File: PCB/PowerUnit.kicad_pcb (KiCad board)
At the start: 2 copper layers, 0 parts

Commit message: added some components
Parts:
- added C1: 1u, erp:C_0805_2012Metric, F.Cu at (205.0, 120.0)
- added C10: 10n, erp:C_0805_2012Metric, F.Cu at (187.4, 118.3)
- added C11: 10n, erp:C_0805_2012Metric, F.Cu at (187.4, 115.4)
- added C12: 10n, erp:C_0805_2012Metric, F.Cu at (197.2, 107.1)
- added C13: 10n, erp:C_0805_2012Metric, F.Cu at (203.5, 102.3)
- added C14: 1u, erp:C_0805_2012Metric, F.Cu at (192.8, 113.3)
- added C15: 220n, erp:C_0805_2012Metric, F.Cu at (197.2, 110.0)
- added C2: 10n, erp:C_0805_2012Metric, F.Cu at (238.0, 104.0)
- added C3: 10n, erp:C_0805_2012Metric, F.Cu at (182.4, 126.7)
- added C4: 100n, erp:C_0805_2012Metric, F.Cu at (191.8, 116.3)
- added C5: 10n, erp:C_0805_2012Metric, F.Cu at (201.6, 105.2)
- added C6: 10n, erp:C_0805_2012Metric, F.Cu at (187.4, 121.3)
- added C7: 10n, erp:C_0805_2012Metric, F.Cu at (211.7, 96.0)
- added C8: 10n, erp:C_0805_2012Metric, F.Cu at (208.0, 99.0)
- added C9: 10u, erp:CP_EIA-6032-15_Kemet-U, F.Cu at (154.4, 125.9)
- added D1: 5.1V, erp:D_MiniMELF, F.Cu at (161.8, 128.4)
- added D19: LL4148, erp:D_MiniMELF, F.Cu at (187.4, 109.0)
- added D2: 5.1V, erp:D_MiniMELF, F.Cu at (201.8, 92.9)
- added D20: LL4148, erp:D_MiniMELF, F.Cu at (168.2, 128.4)
- added D21: LL4148, erp:D_MiniMELF, F.Cu at (198.1, 101.0)
- added D22: LL4148, erp:D_MiniMELF, F.Cu at (177.5, 120.5)
- added D23: GREEN, erp:LED_0805_2012Metric, F.Cu at (192.8, 110.3)
- added D24: RED, erp:LED_0805_2012Metric, F.Cu at (203.6, 99.3)
- added D25: RED, erp:LED_0805_2012Metric, F.Cu at (197.2, 104.1)
- added D26: RED, erp:LED_0805_2012Metric, F.Cu at (178.0, 123.7)
- added D27: RED, erp:LED_0805_2012Metric, F.Cu at (192.8, 107.3)
- added D30: LL4148, erp:D_MiniMELF, F.Cu at (187.4, 112.3)
- added D31: LL4148, erp:D_MiniMELF, F.Cu at (205.0, 81.0)
- added D32: LL4148, erp:D_MiniMELF, F.Cu at (201.8, 96.2)
- added D33: LL4148, erp:D_MiniMELF, F.Cu at (161.8, 125.1)
- added D34: RED, erp:LED_0805_2012Metric, F.Cu at (207.2, 96.1)
- added D35: RED, erp:LED_0805_2012Metric, F.Cu at (229.0, 90.0)
- added D36: RED, erp:LED_0805_2012Metric, F.Cu at (182.5, 123.7)
- added D37: RED, erp:LED_0805_2012Metric, F.Cu at (178.0, 126.7)
- added D8: LL4148, erp:D_MiniMELF, F.Cu at (168.2, 125.1)
- added D9: LL4148, erp:D_MiniMELF, F.Cu at (177.5, 117.3)
- added Q1: BC847C, erp:SOT-23, F.Cu at (182.9, 117.9)
- added Q10: STD45P4LLF6AG, erp:TO-252-3_TabPin2, F.Cu at (156.1, 111.4)
- added Q11: STD45P4LLF6AG, erp:TO-252-3_TabPin2, F.Cu at (165.6, 71.5)
- added Q12: STD15P6F6AG, erp:TO-252-3_TabPin2, F.Cu at (156.1, 103.4)
- added Q13: STD15P6F6AG, erp:TO-252-3_TabPin2, F.Cu at (149.6, 83.5)
- added Q2: STD15P6F6AG, erp:TO-252-3_TabPin2, F.Cu at (168.3, 119.5)
- added Q3: STD45P4LLF6AG, erp:TO-252-3_TabPin2, F.Cu at (192.6, 95.3)
- added Q4: STD45P4LLF6AG, erp:TO-252-3_TabPin2, F.Cu at (180.4, 103.4)
- added Q5: STD15P6F6AG, erp:TO-252-3_TabPin2, F.Cu at (168.3, 111.4)
- added Q6: STD15P6F6AG, erp:TO-252-3_TabPin2, F.Cu at (156.1, 119.5)
- added Q7: STD45P4LLF6AG, erp:TO-252-3_TabPin2, F.Cu at (186.6, 73.5)
- added Q8: BC847C, erp:SOT-23, F.Cu at (173.6, 125.8)
- added Q9: STD15P6F6AG, erp:TO-252-3_TabPin2, F.Cu at (168.3, 103.4)
- added R1: 2.2k, erp:R_0805_2012Metric, F.Cu at (231.0, 121.0)
- added R10: 820, erp:R_0805_2012Metric, F.Cu at (201.6, 111.2)
- added R11: 820, erp:R_0805_2012Metric, F.Cu at (196.2, 116.3)
- added R12: 820, erp:R_0805_2012Metric, F.Cu at (186.9, 127.2)
- added R13: 1k, erp:R_0805_2012Metric, F.Cu at (206.0, 108.2)
- added R14: 2.2k, erp:R_0805_2012Metric, F.Cu at (191.8, 122.2)
- added R15: 2.2k, erp:R_0805_2012Metric, F.Cu at (212.4, 101.9)
- added R16: 2.2k, erp:R_0805_2012Metric, F.Cu at (216.8, 98.8)
- added R17: 820, erp:R_0805_2012Metric, F.Cu at (196.2, 119.2)
- added R18: 820, erp:R_0805_2012Metric, F.Cu at (201.6, 114.1)
- added R19: 2.2k, erp:R_0805_2012Metric, F.Cu at (210.4, 105.0)
- added R2: 2.2k, erp:R_0805_2012Metric, F.Cu at (201.6, 108.2)
- added R20: 2.2k, erp:R_0805_2012Metric, F.Cu at (206.0, 111.2)
- added R21: 820, erp:R_0805_2012Metric, F.Cu at (191.3, 125.1)
- added R22: 820, erp:R_0805_2012Metric, F.Cu at (210.4, 107.9)
- added R23: 820, erp:R_0805_2012Metric, F.Cu at (196.2, 122.2)
- added R24: 2.2k, erp:R_0805_2012Metric, F.Cu at (216.8, 101.7)
- added R25: 2.2k, erp:R_0805_2012Metric, F.Cu at (200.6, 117.0)
- added R26: 2.2k, erp:R_0805_2012Metric, F.Cu at (191.3, 128.1)
- added R27: 2.2k, erp:R_0805_2012Metric, F.Cu at (214.8, 104.9)
- added R28: 560, erp:R_0805_2012Metric, F.Cu at (206.0, 114.1)
- added R29: 2.2k, erp:R_0805_2012Metric, F.Cu at (210.4, 110.8)
- added R3: 2.2k, erp:R_0805_2012Metric, F.Cu at (197.2, 113.0)
- added R30: 2.2k, erp:R_0805_2012Metric, F.Cu at (200.6, 120.0)
- added R31: 2.2k, erp:R_0805_2012Metric, F.Cu at (195.7, 125.1)
- added R32: 2.2k, erp:R_0805_2012Metric, F.Cu at (214.8, 107.8)
- added R33: 2.2k, erp:R_0805_2012Metric, F.Cu at (205.0, 117.0)
- added R34: 2.2k, erp:R_0805_2012Metric, F.Cu at (195.7, 128.1)
- added R35: 2.2k, erp:R_0805_2012Metric, F.Cu at (200.6, 123.0)
- added R36: 2.2k, erp:R_0805_2012Metric, F.Cu at (210.4, 113.8)
- added R4: 2.2k, erp:R_0805_2012Metric, F.Cu at (208.0, 102.0)
- added R5: 1k, erp:R_0805_2012Metric, F.Cu at (212.4, 99.0)
- added R6: 1k, erp:R_0805_2012Metric, F.Cu at (191.8, 119.2)
- added R7: 820, erp:R_0805_2012Metric, F.Cu at (206.0, 105.2)
- added R8: 2.2k, erp:R_0805_2012Metric, F.Cu at (186.9, 124.2)
- added R9: 820, erp:R_0805_2012Metric, F.Cu at (238.0, 98.0)
- added U1: STM8S001J3M3, erp:SOIC-8_3.9x4.9mm_P1.27mm, F.Cu at (190.7, 102.6)
- added U2: L5150BN, erp:SOT-223-3_TabPin2, F.Cu at (179.3, 111.5)

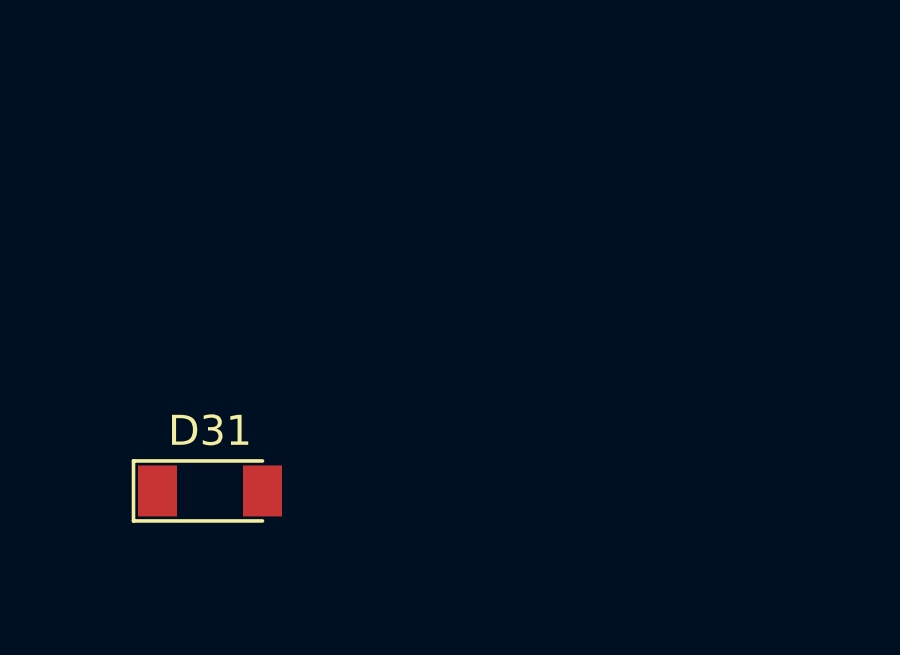
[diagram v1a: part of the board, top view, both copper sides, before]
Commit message: Added SWIM connector
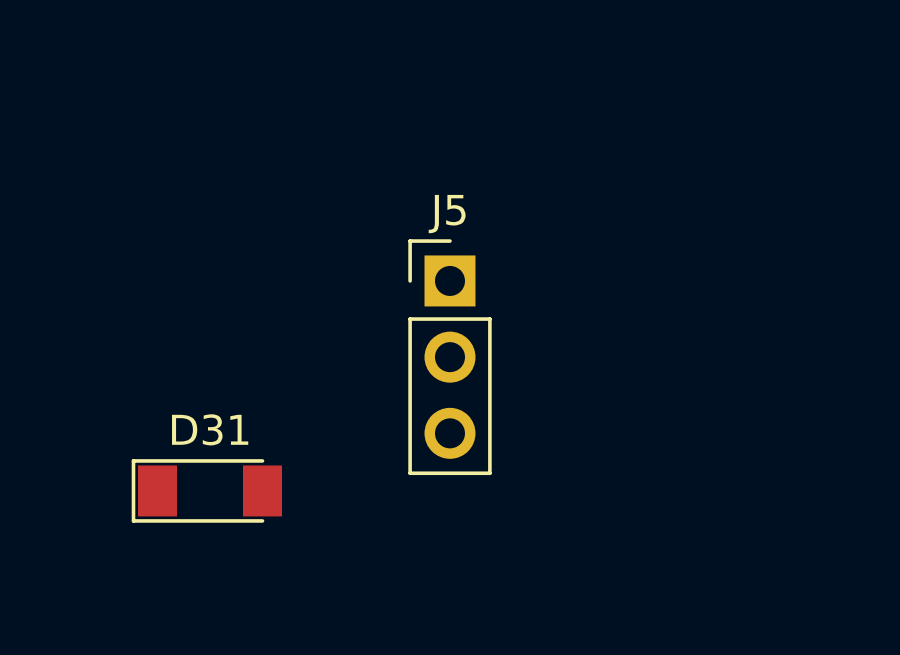
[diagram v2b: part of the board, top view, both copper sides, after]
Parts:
- added J5: CON-3, erp:PinHeader_1x03_P2.54mm_Vertical, F.Cu at (213.0, 74.0)
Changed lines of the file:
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@@
     (tracks 0)
     (zones 0)
-    (modules 87)
+    (modules 88)
     (nets 52)
   )
@@
     (add_net "Net-(Q8-Pad3)")
   )
+  (module erp:PinHeader_1x03_P2.54mm_Vertical (layer F.Cu)
+    (at 213 74)
+    (descr "Through hole straight pin header, 1x03, 2.54mm pitch, single row")
+    (tags "Through hole pin header THT 1x03 2.54mm single row")
+    (fp_text reference J5 (at 0 -2.33) (layer F.SilkS)
+      (effects (font (size 1 1) (thickness 0.15)))
+    )
+    (fp_text value CON-3 (at 0 7.41) (layer F.Fab)
+      (effects (font (size 1 1) (thickness 0.15)))
+    )
+    (fp_text user %R (at 0 2.54 90) (layer F.Fab)
+      (effects (font (size 1 1) (thickness 0.15)))
+    )
+    (fp_line (start 1.8 -1.8) (end -1.8 -1.8) (layer F.CrtYd) (width 0.05))
+    (fp_line (start 1.8 6.85) (end 1.8 -1.8) (layer F.CrtYd) (width 0.05))
+    (fp_line (start -1.8 6.85) (end 1.8 6.85) (layer F.CrtYd) (width 0.05))
+    (fp_line (start -1.8 -1.8) (end -1.8 6.85) (layer F.CrtYd) (width 0.05))
+    (fp_line (start -1.33 -1.33) (end 0 -1.33) (layer F.SilkS) (width 0.12))
+    (fp_line (start -1.33 0) (end -1.33 -1.33) (layer F.SilkS) (width 0.12))
+    (fp_line (start -1.33 1.27) (end 1.33 1.27) (layer F.SilkS) (width 0.12))
+    (fp_line (start 1.33 1.27) (end 1.33 6.41) (layer F.SilkS) (width 0.12))
+    (fp_line (start -1.33 1.27) (end -1.33 6.41) (layer F.SilkS) (width 0.12))
+    (fp_line (start -1.33 6.41) (end 1.33 6.41) (layer F.SilkS) (width 0.12))
+    (fp_line (start -1.27 -0.635) (end -0.635 -1.27) (layer F.Fab) (width 0.1))
+    (fp_line (start -1.27 6.35) (end -1.27 -0.635) (layer F.Fab) (width 0.1))
+    (fp_line (start 1.27 6.35) (end -1.27 6.35) (layer F.Fab) (width 0.1))
+    (fp_line (start 1.27 -1.27) (end 1.27 6.35) (layer F.Fab) (width 0.1))
+    (fp_line (start -0.635 -1.27) (end 1.27 -1.27) (layer F.Fab) (width 0.1))
+    (pad 3 thru_hole oval (at 0 5.08) (size 1.7 1.7) (drill 1) (layers *.Cu *.Mask)
+      (net 5 +5V))
+    (pad 2 thru_hole oval (at 0 2.54) (size 1.7 1.7) (drill 1) (layers *.Cu *.Mask)
+      (net 50 /SWIM))
+    (pad 1 thru_hole rect (at 0 0) (size 1.7 1.7) (drill 1) (layers *.Cu *.Mask)
+      (net 1 GND))
+    (model ${KISYS3DMOD}/Connector_PinHeader_2.54mm.3dshapes/PinHeader_1x03_P2.54mm_Vertical.wrl
+      (at (xyz 0 0 0))
+      (scale (xyz 1 1 1))
+      (rotate (xyz 0 0 0))
+    )
+  )
   (module erp:SOT-223-3_TabPin2 (layer F.Cu)

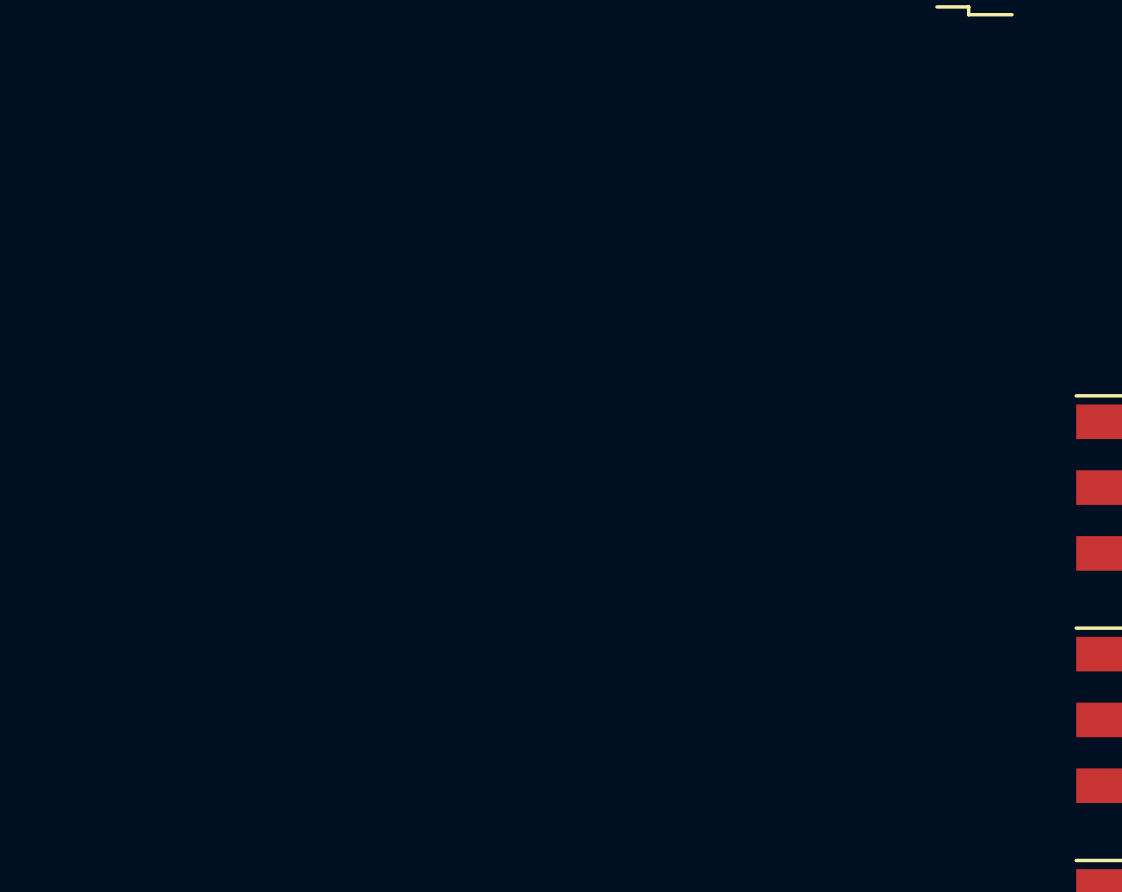
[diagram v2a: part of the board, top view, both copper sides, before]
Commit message: Changed TVS diodes
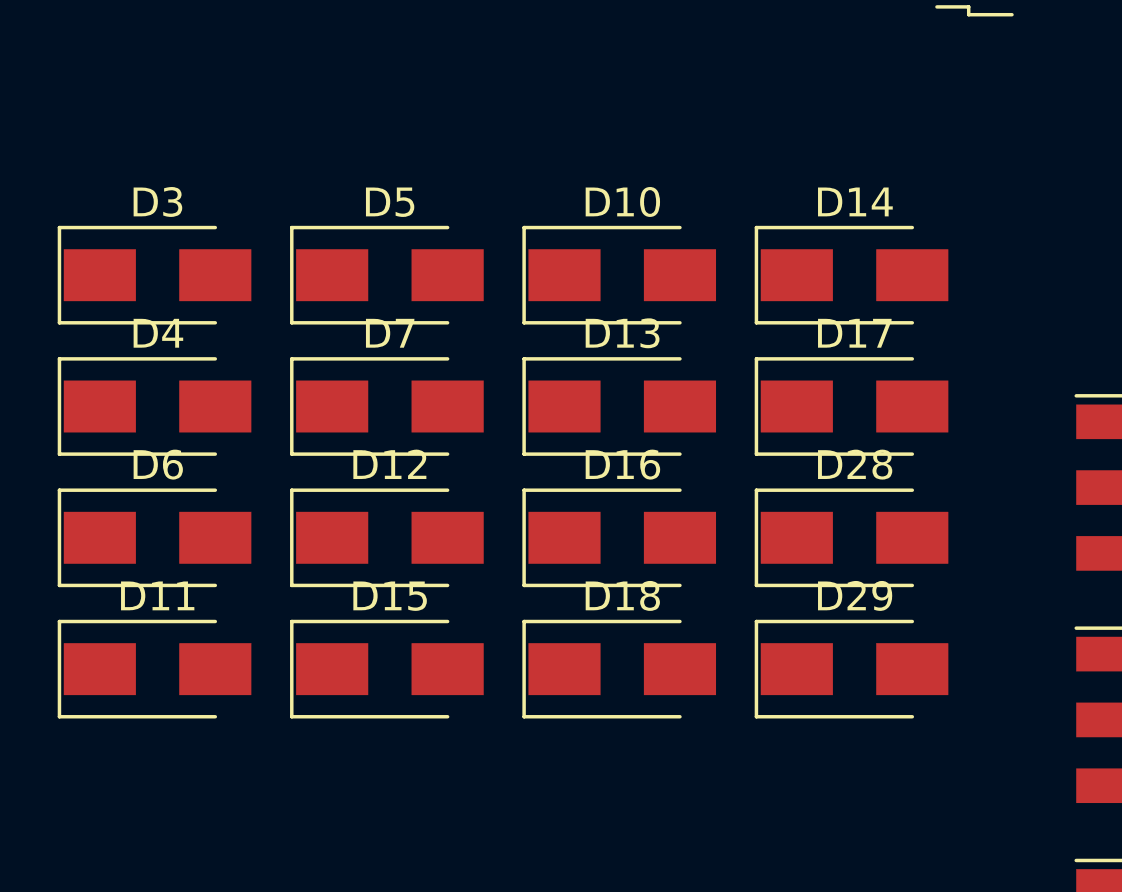
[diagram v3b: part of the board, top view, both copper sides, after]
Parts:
- added D10: SMA6F15AY, erp:D_SMA, F.Cu at (135.1, 96.0)
- added D11: SMA6F15AY, erp:D_SMA, F.Cu at (119.0, 109.7)
- added D12: SMA6F15AY, erp:D_SMA, F.Cu at (127.0, 105.1)
- added D13: SMA6F15AY, erp:D_SMA, F.Cu at (135.1, 100.5)
- added D14: SMA6F15AY, erp:D_SMA, F.Cu at (143.2, 96.0)
- added D15: SMA6F15AY, erp:D_SMA, F.Cu at (127.0, 109.7)
- added D16: SMA6F15AY, erp:D_SMA, F.Cu at (135.1, 105.1)
- added D17: SMA6F15AY, erp:D_SMA, F.Cu at (143.2, 100.5)
- added D18: SMA6F15AY, erp:D_SMA, F.Cu at (135.1, 109.7)
- added D28: SMA6F15AY, erp:D_SMA, F.Cu at (143.2, 105.1)
- added D29: SMA6F15AY, erp:D_SMA, F.Cu at (143.2, 109.7)
- added D3: SMA6F15AY, erp:D_SMA, F.Cu at (119.0, 96.0)
- added D4: SMA6F15AY, erp:D_SMA, F.Cu at (119.0, 100.5)
- added D5: SMA6F15AY, erp:D_SMA, F.Cu at (127.0, 96.0)
- added D6: SMA6F15AY, erp:D_SMA, F.Cu at (119.0, 105.1)
- added D7: SMA6F15AY, erp:D_SMA, F.Cu at (127.0, 100.5)
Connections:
- D30 pad 2: (no net) -> /PWD_ECU

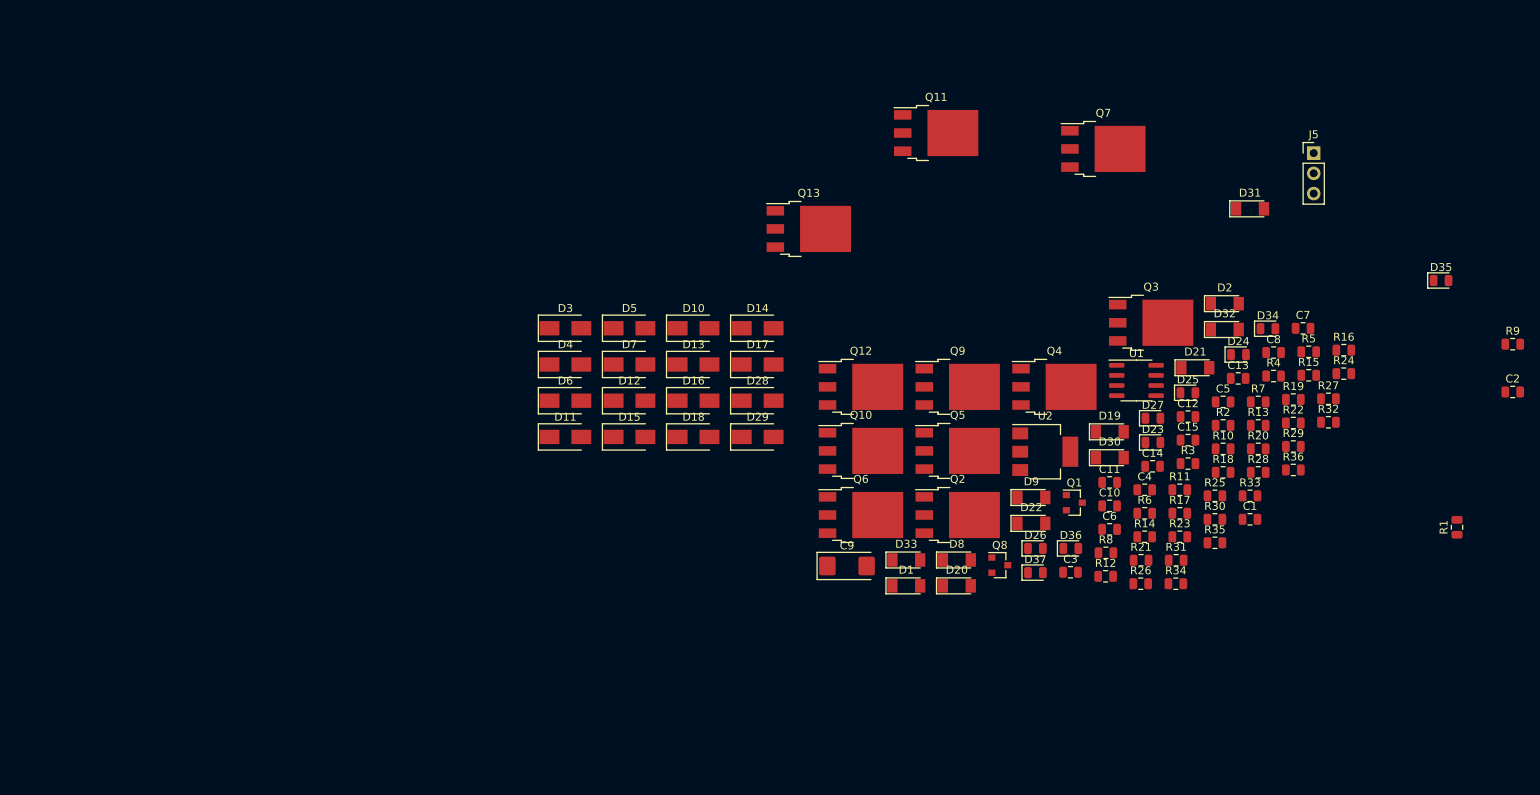
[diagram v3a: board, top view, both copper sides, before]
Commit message: All footprints added
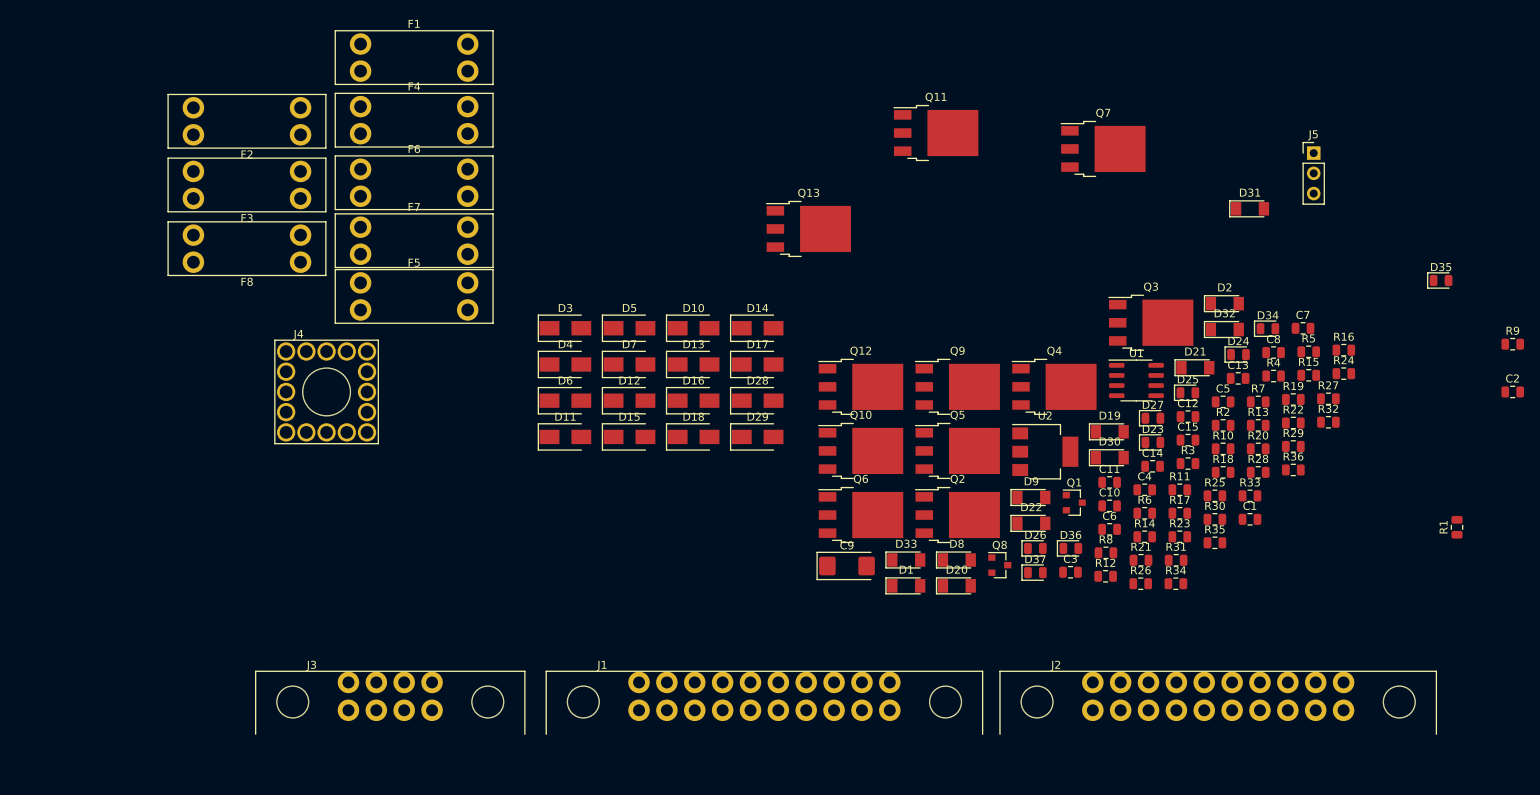
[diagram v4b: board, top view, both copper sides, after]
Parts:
- added F1: FUSE, erp:Keystone_FuseHolder, F.Cu at (100.0, 62.0)
- added F2: FUSE, erp:Keystone_FuseHolder, F.Cu at (79.0, 70.0)
- added F3: FUSE, erp:Keystone_FuseHolder, F.Cu at (79.0, 78.0)
- added F4: FUSE, erp:Keystone_FuseHolder, F.Cu at (100.0, 69.9)
- added F5: FUSE, erp:Keystone_FuseHolder, F.Cu at (100.0, 92.0)
- added F6: FUSE, erp:Keystone_FuseHolder, F.Cu at (100.0, 77.7)
- added F7: FUSE, erp:Keystone_FuseHolder, F.Cu at (100.0, 85.0)
- added F8: FUSE, erp:Keystone_FuseHolder, F.Cu at (79.0, 86.0)
- added J1: MX150-20, erp:Molex_MX150_2x10_Header, F.Cu at (144.0, 147.0)
- added J2: MX150-20, erp:Molex_MX150_2x10_Header, F.Cu at (201.0, 147.0)
- added J3: MX150-8, erp:Molex_MX150_2x04_Header, F.Cu at (97.0, 147.0)
- added J4: REDCUBE, erp:Wurth_WP-BUCF_M6, F.Cu at (89.0, 104.0)
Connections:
- D8 pad 1: (no net) -> /IN_FAN_A
- D9 pad 1: (no net) -> /IN_FAN_B
- R10 pad 2: (no net) -> /IN_AUX
- R11 pad 2: (no net) -> /IN_RAIN
- R12 pad 2: (no net) -> /IN_BRAKE
- R21 pad 2: (no net) -> /IN_IGN
- R22 pad 2: (no net) -> /IN_FUEL
- R23 pad 2: (no net) -> /IN_LIGHT
- R9 pad 2: (no net) -> /IN_INJECT
